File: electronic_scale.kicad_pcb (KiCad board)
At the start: 2 copper layers, 53 x 49 mm, 57 parts, among them J1 USB_C_Receptacle_USB2.0_16P, J2 Conn_01x02_MountingPin, J3 Conn_01x04_Socket, J4 Conn_01x04_Pin, J5 Conn_01x04_Pin, Q1 Si2305CDS, Q2 Si2305CDS, Q3 SS8050, Q4 SS8550, SW1 SW_Push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

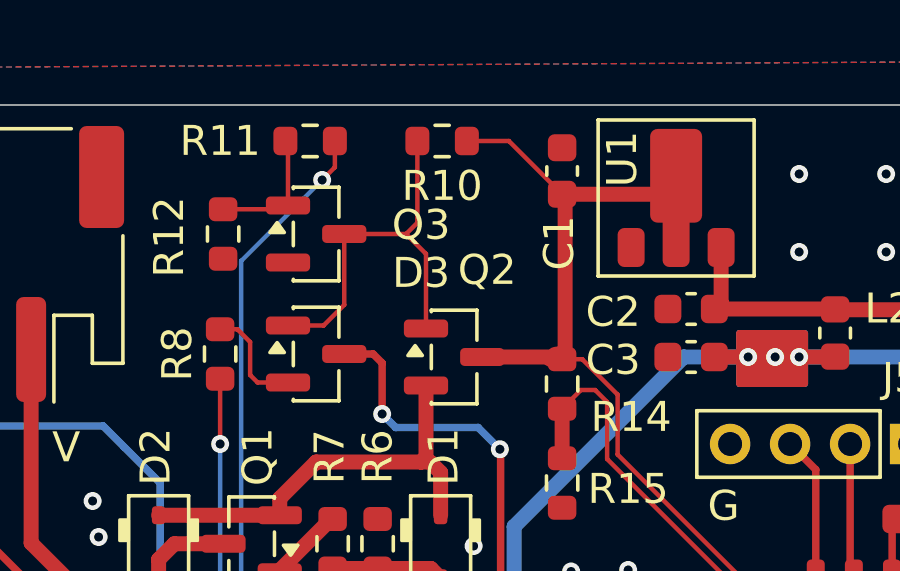
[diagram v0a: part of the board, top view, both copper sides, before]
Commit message: 更正电源开关电路的原理错误
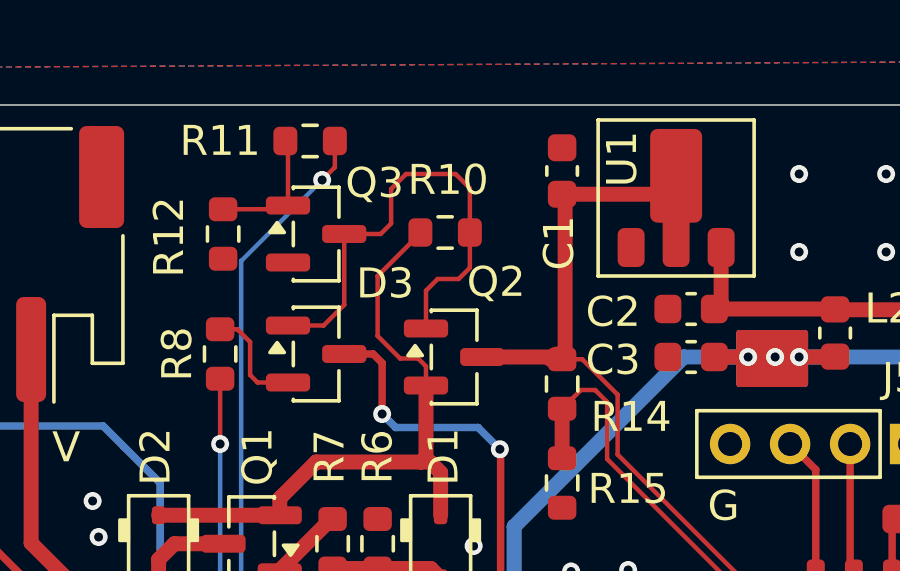
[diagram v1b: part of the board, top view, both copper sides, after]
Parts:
- moved R10 3.05 mm to (149.7, 88.8), turned to 0 degrees
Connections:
- R10 pad 1: VCC -> Net-(D1-K)
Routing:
- net Net-(D1-K): track 14.7 -> 21.4 mm
- net VCC: track 33.9 -> 30.0 mm
- net Net-(D3-A2): track 13.3 -> 16.1 mm
